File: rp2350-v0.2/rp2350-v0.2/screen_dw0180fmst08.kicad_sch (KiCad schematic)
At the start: 15 parts, among them J4 DO0180FMST08

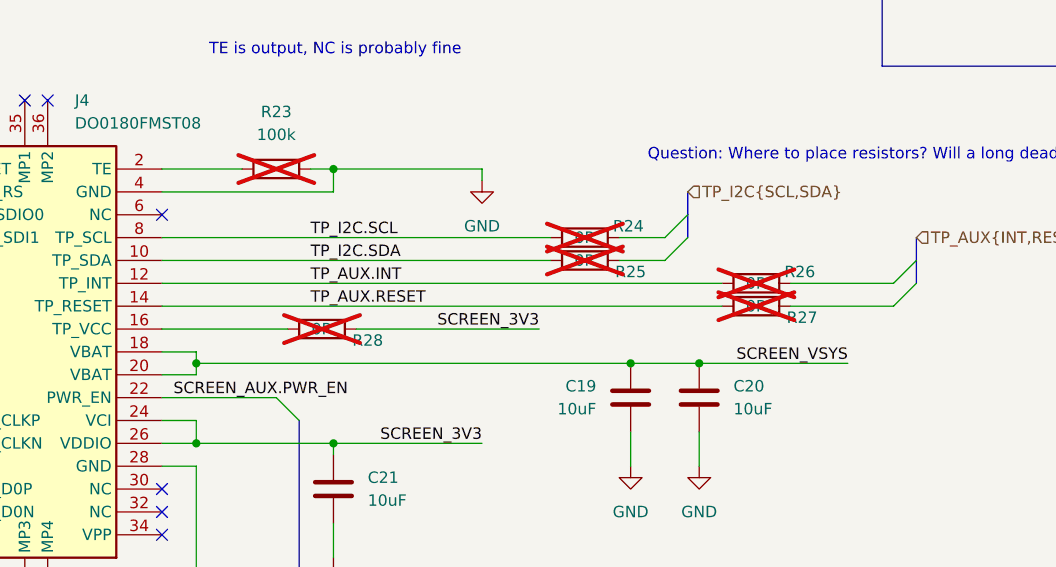
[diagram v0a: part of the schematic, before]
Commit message: v0.2: schematic draft 1 done
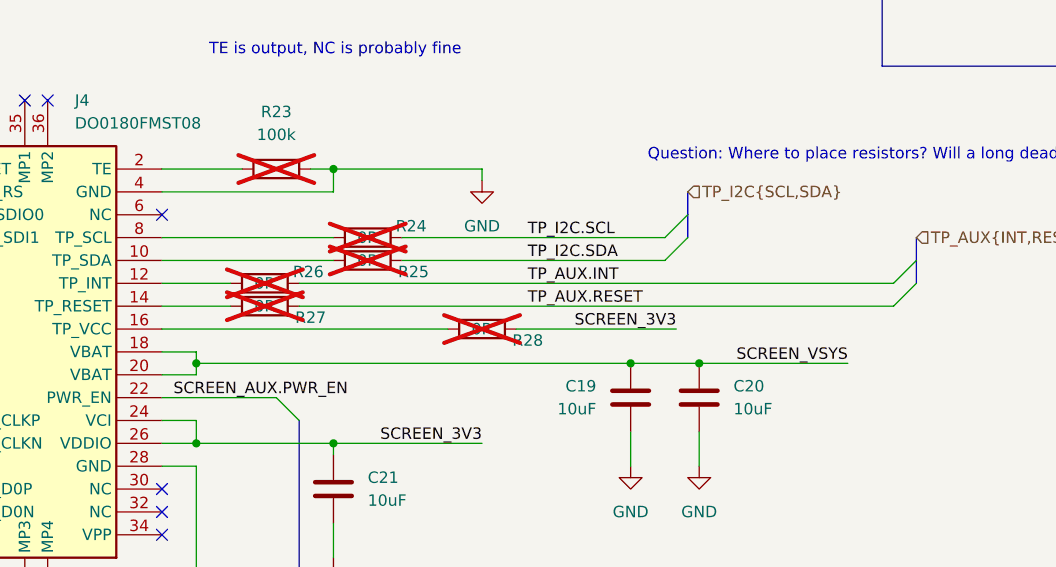
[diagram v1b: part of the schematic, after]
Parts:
- JP4, JP5: footprint (none) -> CustomFootprints:BridgedJumper_P2.54mm
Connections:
- net TP_AUX.INT: now also R26.2; no longer J4.12 (TP_INT), R26.1
- net TP_AUX.RESET: now also R27.2; no longer J4.14 (TP_RESET), R27.1
- net TP_I2C.SCL: now also R24.2; no longer J4.8 (TP_SCL), R24.1
- net TP_I2C.SDA: now also R25.2; no longer J4.10 (TP_SDA), R25.1
- new net: J4.10 (TP_SDA), R25.1
- new net: J4.12 (TP_INT), R26.1
- new net: J4.8 (TP_SCL), R24.1
- new net: J4.14 (TP_RESET), R27.1
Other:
- moved on the sheet: R24, R25, R26, R27, R28
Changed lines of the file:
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@@
 	(wire
 		(pts
-			(xy 148.59 105.41) (xy 168.91 105.41)
+			(xy 166.37 105.41) (xy 184.15 105.41)
 		)
 		(stroke
@@
 	(wire
 		(pts
-			(xy 196.85 100.33) (xy 208.28 100.33)
-		)
-		(stroke
-			(width 0)
-			(type default)
-		)
-	)
-	(wire
-		(pts
 			(xy 127 87.63) (xy 135.89 87.63)
 		)
@@
 	(wire
 		(pts
-			(xy 177.8 97.79) (xy 182.88 97.79)
+			(xy 153.67 97.79) (xy 182.88 97.79)
 		)
 		(stroke
@@
 	(wire
 		(pts
-			(xy 127 102.87) (xy 189.23 102.87)
+			(xy 127 102.87) (xy 134.62 102.87)
 		)
 		(stroke
@@
 	(wire
 		(pts
-			(xy 196.85 102.87) (xy 208.28 102.87)
+			(xy 142.24 102.87) (xy 208.28 102.87)
 		)
 		(stroke
@@
 	(wire
 		(pts
+			(xy 142.24 100.33) (xy 208.28 100.33)
+		)
+		(stroke
+			(width 0)
+			(type default)
+		)
+	)
+	(wire
+		(pts
 			(xy 81.28 105.41) (xy 99.06 105.41)
 		)
@@
 	(wire
 		(pts
-			(xy 127 97.79) (xy 170.18 97.79)
+			(xy 127 97.79) (xy 146.05 97.79)
 		)
 		(stroke
@@
 	(wire
 		(pts
-			(xy 127 105.41) (xy 140.97 105.41)
+			(xy 127 105.41) (xy 158.75 105.41)
 		)
 		(stroke
@@
 	(wire
 		(pts
-			(xy 177.8 95.25) (xy 182.88 95.25)
+			(xy 153.67 95.25) (xy 182.88 95.25)
 		)
 		(stroke
@@
 	(wire
 		(pts
-			(xy 127 100.33) (xy 189.23 100.33)
+			(xy 127 100.33) (xy 134.62 100.33)
 		)
 		(stroke
@@
 	(wire
 		(pts
-			(xy 127 95.25) (xy 170.18 95.25)
+			(xy 127 95.25) (xy 146.05 95.25)
 		)
 		(stroke
@@
 	)
 	(label "SCREEN_3V3"
-		(at 168.91 105.41 180)
+		(at 184.15 105.41 180)
 		(effects
 			(font
@@
 			)
 			(justify right bottom)
+		)
+	)
+	(label "TP_AUX.RESET"
+		(at 167.64 102.87 0)
+		(effects
+			(font
+				(size 1.27 1.27)
+			)
+			(justify left bottom)
 		)
 	)
@@
 		)
 	)
-	(label "TP_AUX.RESET"
-		(at 143.51 102.87 0)
+	(label "TP_AUX.INT"
+		(at 167.64 100.33 0)
 		(effects
 			(font
@@
 		)
 	)
-	(label "TP_AUX.INT"
-		(at 143.51 100.33 0)
-		(effects
-			(font
-				(size 1.27 1.27)
-			)
-			(justify left bottom)
-		)
-	)
 	(label "TP_I2C.SCL"
-		(at 143.51 95.25 0)
+		(at 167.64 95.25 0)
 		(effects
 			(font
@@
 		)
 	)
-	(label "TP_I2C.SDA"
-		(at 143.51 97.79 0)
-		(effects
-			(font
-				(size 1.27 1.27)
-			)
-			(justify left bottom)
-		)
-	)
 	(label "QSPI.SDIO3"
 		(at 88.9 105.41 0)
@@
 			)
 			(justify right bottom)
+		)
+	)
+	(label "TP_I2C.SDA"
+		(at 167.64 97.79 0)
+		(effects
+			(font
+				(size 1.27 1.27)
+			)
+			(justify left bottom)
 		)
 	)
@@
 	(symbol
 		(lib_id "Device:R")
-		(at 173.99 97.79 90)
+		(at 149.86 97.79 90)
 		(unit 1)
 		(exclude_from_sim no)
@@
 		(dnp yes)
 		(property "Reference" "R25"
-			(at 179.07 99.06 90)
+			(at 154.94 99.06 90)
 			(effects
 				(font
@@
 		)
 		(property "Value" "0R"
-			(at 173.99 97.79 90)
+			(at 149.86 97.79 90)
 			(effects
 				(font
@@
 		)
 		(property "Footprint" "Resistor_SMD:R_0603_1608Metric"
-			(at 173.99 99.568 90)
+			(at 149.86 99.568 90)
 			(effects
 				(font
@@
 		)
 		(property "Datasheet" "~"
-			(at 173.99 97.79 0)
+			(at 149.86 97.79 0)
 			(effects
 				(font
@@
 		)
 		(property "Description" "Resistor"
-			(at 173.99 97.79 0)
+			(at 149.86 97.79 0)
 			(effects
 				(font
@@
 	(symbol
 		(lib_id "Device:R")
-		(at 193.04 100.33 90)
+		(at 138.43 100.33 90)
 		(unit 1)
 		(exclude_from_sim no)
@@
 		(dnp yes)
 		(property "Reference" "R26"
-			(at 197.866 99.06 90)
+			(at 143.256 99.06 90)
 			(effects
 				(font
@@
 		)
 		(property "Value" "0R"
-			(at 193.04 100.33 90)
+			(at 138.43 100.33 90)
 			(effects
 				(font
@@
 		)
 		(property "Footprint" "Resistor_SMD:R_0603_1608Metric"
-			(at 193.04 102.108 90)
+			(at 138.43 102.108 90)
 			(effects
 				(font
@@
 		)
 		(property "Datasheet" "~"
-			(at 193.04 100.33 0)
+			(at 138.43 100.33 0)
 			(effects
 				(font
@@
 		)
 		(property "Description" "Resistor"
-			(at 193.04 100.33 0)
+			(at 138.43 100.33 0)
 			(effects
 				(font
@@
 	(symbol
 		(lib_id "Device:R")
-		(at 173.99 95.25 90)
+		(at 149.86 95.25 90)
 		(unit 1)
 		(exclude_from_sim no)
@@
 		(dnp yes)
 		(property "Reference" "R24"
-			(at 178.816 93.98 90)
+			(at 154.686 93.98 90)
 			(effects
 				(font
@@
 		)
 		(property "Value" "0R"
-			(at 173.99 95.25 90)
+			(at 149.86 95.25 90)
 			(effects
 				(font
@@
 		)
 		(property "Footprint" "Resistor_SMD:R_0603_1608Metric"
-			(at 173.99 97.028 90)
+			(at 149.86 97.028 90)
 			(effects
 				(font
@@
 		)
 		(property "Datasheet" "~"
-			(at 173.99 95.25 0)
+			(at 149.86 95.25 0)
 			(effects
 				(font
@@
 		)
 		(property "Description" "Resistor"
-			(at 173.99 95.25 0)
+			(at 149.86 95.25 0)
 			(effects
 				(font
@@
 			)
 		)
-		(property "Footprint" ""
+		(property "Footprint" "CustomFootprints:BridgedJumper_P2.54mm"
 			(at 231.14 41.91 0)
 			(effects
@@
 	(symbol
 		(lib_id "Device:R")
-		(at 193.04 102.87 90)
+		(at 138.43 102.87 90)
 		(unit 1)
 		(exclude_from_sim no)
@@
 		(dnp yes)
 		(property "Reference" "R27"
-			(at 198.12 104.14 90)
+			(at 143.51 104.14 90)
 			(effects
 				(font
@@
 		)
 		(property "Value" "0R"
-			(at 193.04 102.87 90)
+			(at 138.43 102.87 90)
 			(effects
 				(font
@@
 		)
 		(property "Footprint" "Resistor_SMD:R_0603_1608Metric"
-			(at 193.04 104.648 90)
+			(at 138.43 104.648 90)
 			(effects
 				(font
@@
 		)
 		(property "Datasheet" "~"
-			(at 193.04 102.87 0)
+			(at 138.43 102.87 0)
 			(effects
 				(font
@@
 		)
 		(property "Description" "Resistor"
-			(at 193.04 102.87 0)
+			(at 138.43 102.87 0)
 			(effects
 				(font
@@
 			)
 		)
-		(property "Footprint" ""
+		(property "Footprint" "CustomFootprints:BridgedJumper_P2.54mm"
 			(at 232.41 60.96 0)
 			(effects
@@
 	(symbol
 		(lib_id "Device:R")
-		(at 144.78 105.41 90)
+		(at 162.56 105.41 90)
 		(unit 1)
 		(exclude_from_sim no)
@@
 		(dnp yes)
 		(property "Reference" "R28"
-			(at 149.86 106.68 90)
+			(at 167.64 106.68 90)
 			(effects
 				(font
@@
 		)
 		(property "Value" "0R"
-			(at 144.78 105.41 90)
+			(at 162.56 105.41 90)
 			(effects
 				(font
@@
 		)
 		(property "Footprint" "Resistor_SMD:R_0603_1608Metric"
-			(at 144.78 107.188 90)
+			(at 162.56 107.188 90)
 			(effects
 				(font
@@
 		)
 		(property "Datasheet" "~"
-			(at 144.78 105.41 0)
+			(at 162.56 105.41 0)
 			(effects
 				(font
@@
 		)
 		(property "Description" "Resistor"
-			(at 144.78 105.41 0)
-			(effects
-				(font
+			(at 162.56 105.41 0)
+			(effects
+				(font

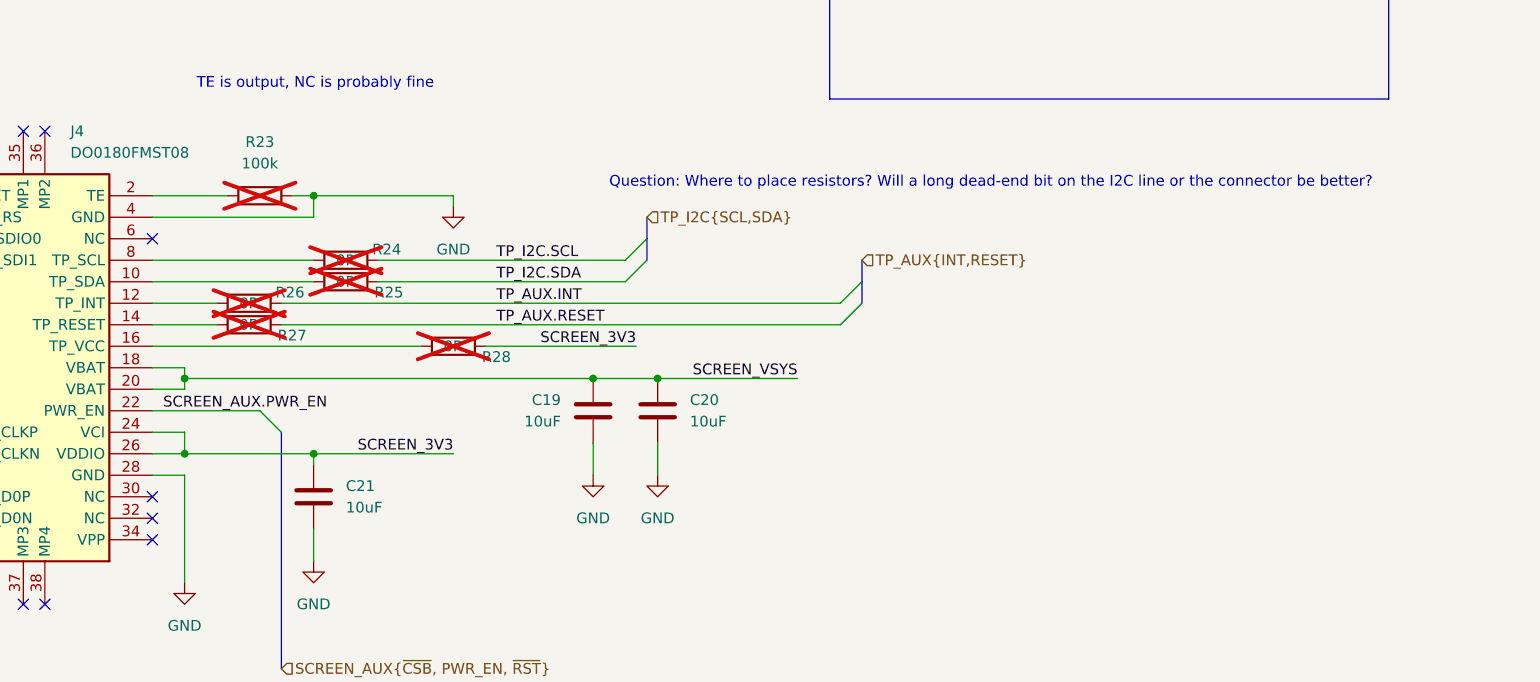
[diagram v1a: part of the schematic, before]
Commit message: v0.2: more progress on routing, nearly done
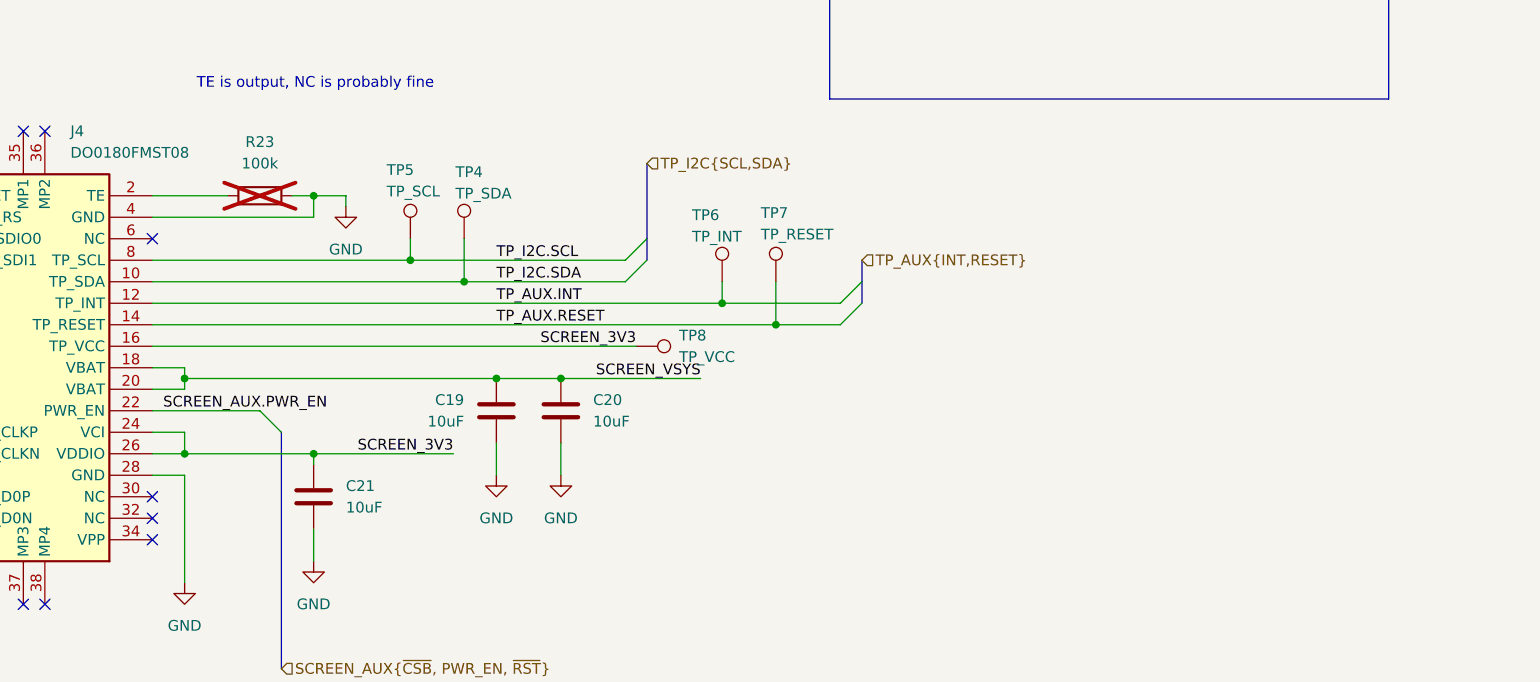
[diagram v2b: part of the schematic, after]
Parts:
- removed R24, R25, R26, R27, R28: 0R, Resistor_SMD:R_0603_1608Metric, symbol Device:R
- added TP4: TP_SDA, TestPoint:TestPoint_Pad_1.0x1.0mm, symbol Connector:TestPoint
- added TP5: TP_SCL, TestPoint:TestPoint_Pad_1.0x1.0mm, symbol Connector:TestPoint
- added TP6: TP_INT, TestPoint:TestPoint_Pad_1.0x1.0mm, symbol Connector:TestPoint
- added TP7: TP_RESET, TestPoint:TestPoint_Pad_1.0x1.0mm, symbol Connector:TestPoint
- added TP8: TP_VCC, TestPoint:TestPoint_Pad_1.0x1.0mm, symbol Connector:TestPoint
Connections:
- net SCREEN_3V3: now also J4.16 (TP_VCC), TP8.1
- net TP_AUX.INT: now also J4.12 (TP_INT), TP6.1
- net TP_AUX.RESET: now also J4.14 (TP_RESET), TP7.1
- net TP_I2C.SCL: now also J4.8 (TP_SCL), TP5.1
- net TP_I2C.SDA: now also J4.10 (TP_SDA), TP4.1
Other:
- note removed: "Question: Where to place resistors? Will a long dead-end bit on the I2C line or the connector be better?"
- moved on the sheet: C19, C20

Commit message: v0.2: routing done, nearly ready for prod
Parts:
- JP4: value SCREEN_IO_PWR -> IO_PWR
- JP5: value SCREEN_PANEL_PWR -> PANEL_PWR
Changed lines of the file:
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@@
 			)
 		)
-		(property "Value" "SCREEN_IO_PWR"
+		(property "Value" "IO_PWR"
 			(at 231.14 39.37 0)
 			(effects
@@
 			)
 		)
-		(property "Value" "SCREEN_PANEL_PWR"
+		(property "Value" "PANEL_PWR"
 			(at 232.41 58.42 0)
 			(effects

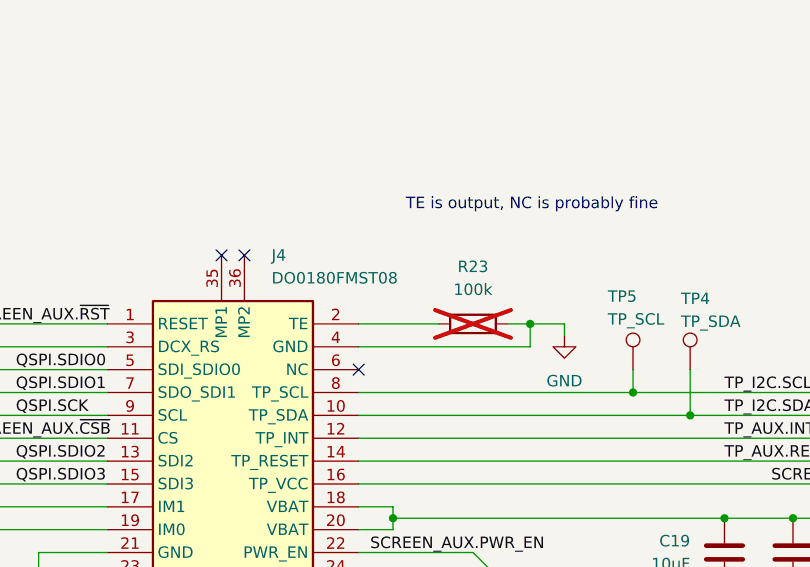
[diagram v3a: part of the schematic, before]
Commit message: v0.2: update battery connector and labels
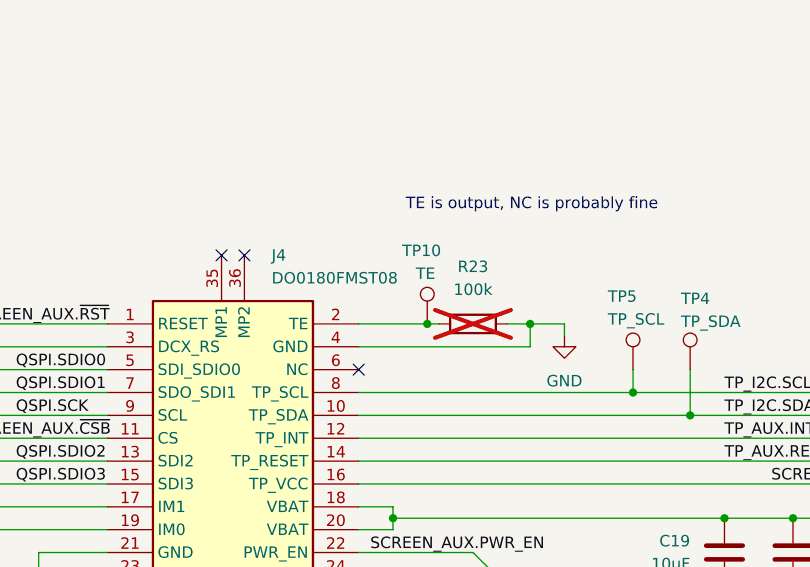
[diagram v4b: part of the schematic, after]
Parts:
- added TP10: TE, TestPoint:TestPoint_Pad_1.0x1.0mm, symbol Connector:TestPoint
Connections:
- net at J4.2 (TE), R23.1: now also TP10.1
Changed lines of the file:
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@@
+	)
+	(junction
+		(at 134.62 87.63)
+		(diameter 0)
+		(color 0 0 0 0)
 	)
 	(junction
@@
 	(wire
 		(pts
-			(xy 127 87.63) (xy 135.89 87.63)
+			(xy 127 87.63) (xy 134.62 87.63)
 		)
 		(stroke
@@
 		(pts
 			(xy 78.74 92.71) (xy 78.74 95.25)
+		)
+		(stroke
+			(width 0)
+			(type default)
+		)
+	)
+	(wire
+		(pts
+			(xy 134.62 87.63) (xy 135.89 87.63)
 		)
 		(stroke
@@
 					(unit 1)
 				)
+			)
+		)
+	)
+	(symbol
+		(lib_id "Connector:TestPoint")
+		(at 134.62 87.63 0)
+		(unit 1)
+		(exclude_from_sim no)
+		(in_bom yes)
+		(on_board yes)
+		(dnp no)
+		(property "Reference" "TP10"
+			(at 131.826 79.502 0)
+			(effects
+				(font
+					(size 1.27 1.27)
+				)
+				(justify left)
+			)
+		)
+		(property "Value" "TE"
+			(at 133.35 82.042 0)
+			(effects
+				(font
+					(size 1.27 1.27)
+				)
+				(justify left)
+			)
+		)
+		(property "Footprint" "TestPoint:TestPoint_Pad_1.0x1.0mm"
+			(at 139.7 87.63 0)
+			(effects
+				(font
+					(size 1.27 1.27)
+				)
+				(hide yes)
+			)
+		)
+		(property "Datasheet" "~"
+			(at 139.7 87.63 0)
+			(effects
+				(font
+					(size 1.27 1.27)
+				)
+				(hide yes)
+			)
+		)
+		(property "Description" "test point"
+			(at 134.62 87.63 0)
+			(effects
+				(font
+					(size 1.27 1.27)
+				)
+				(hide yes)
+			)
+		)
+		(pin "1"
+		)
+		(instances
+			(project "rp2350-v0.2"
+				(path "/5cbb45d4-7f83-48dd-a53b-5c75c7d1d827/acc6b550-0215-4302-88ee-d8cdb26529cb"
+					(reference "TP10")
+					(unit 1)
+				)

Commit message: v0.2: sent to jlc
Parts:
- R22: footprint Resistor_SMD:R_0402_1005Metric -> Resistor_SMD:R_0603_1608Metric
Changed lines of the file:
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@@
 			)
 		)
-		(property "Footprint" "Resistor_SMD:R_0402_1005Metric"
+		(property "Footprint" "Resistor_SMD:R_0603_1608Metric"
 			(at 66.802 95.25 90)
 			(effects
